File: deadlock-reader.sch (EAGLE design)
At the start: 57 parts, among them IC1 LM386M-1, IC2 STM32F072XX, IC3 MCP16301/H, IC4 MAX3232CSE, J1 RJ11-2X, X1 MINI-USB-SCHIELD-32005-301

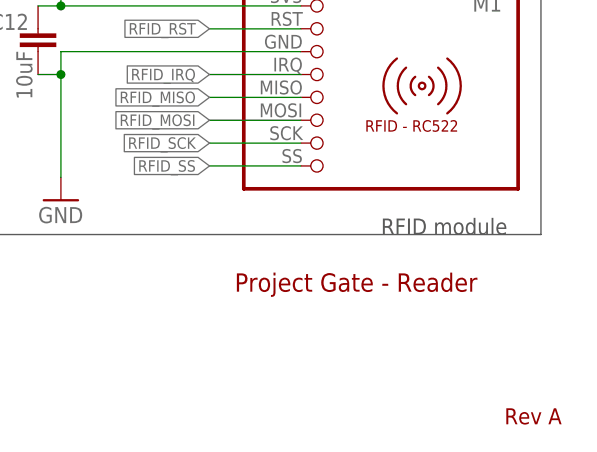
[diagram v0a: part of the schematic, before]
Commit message: Remove all occurences of name 'Gate'
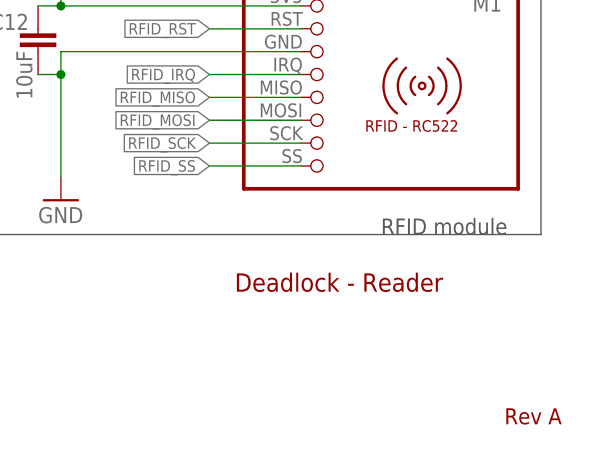
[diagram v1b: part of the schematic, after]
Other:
- note added: "Deadlock - Reader"
- note removed: "Project Gate - Reader"
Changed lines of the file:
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@@
 <?xml version="1.0" encoding="utf-8"?>
 <!DOCTYPE eagle SYSTEM "eagle.dtd">
-<eagle version="7.2.0">
+<eagle version="7.3.0">
 <drawing>
 <settings>
@@
 <sheet>
 <plain>
-<text x="217.424" y="20.32" size="2.032" layer="94" font="vector">Project Gate - Reader</text>
+<text x="217.424" y="20.32" size="2.032" layer="94" font="vector">Deadlock - Reader</text>
 <text x="247.396" y="5.588" size="1.778" layer="94" font="vector">Rev A</text>
 <wire x1="154.94" y1="170.18" x2="251.46" y2="170.18" width="0.1524" layer="97"/>

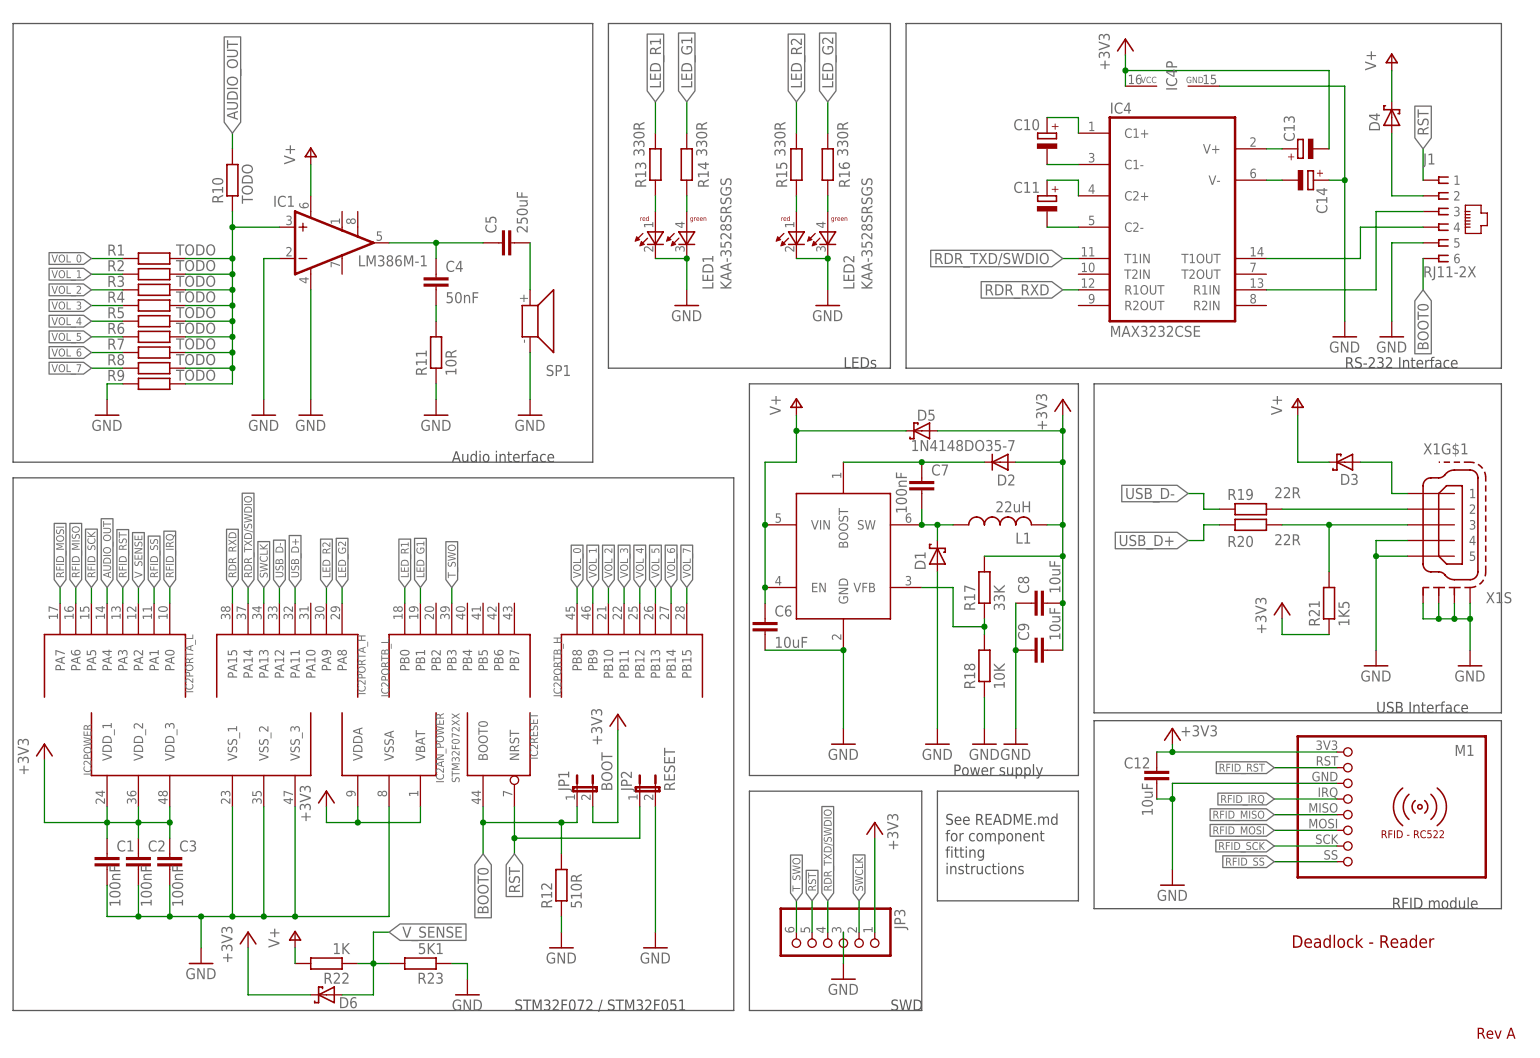
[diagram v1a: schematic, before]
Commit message: User trimmer to regulate audio volume instead of digital pot
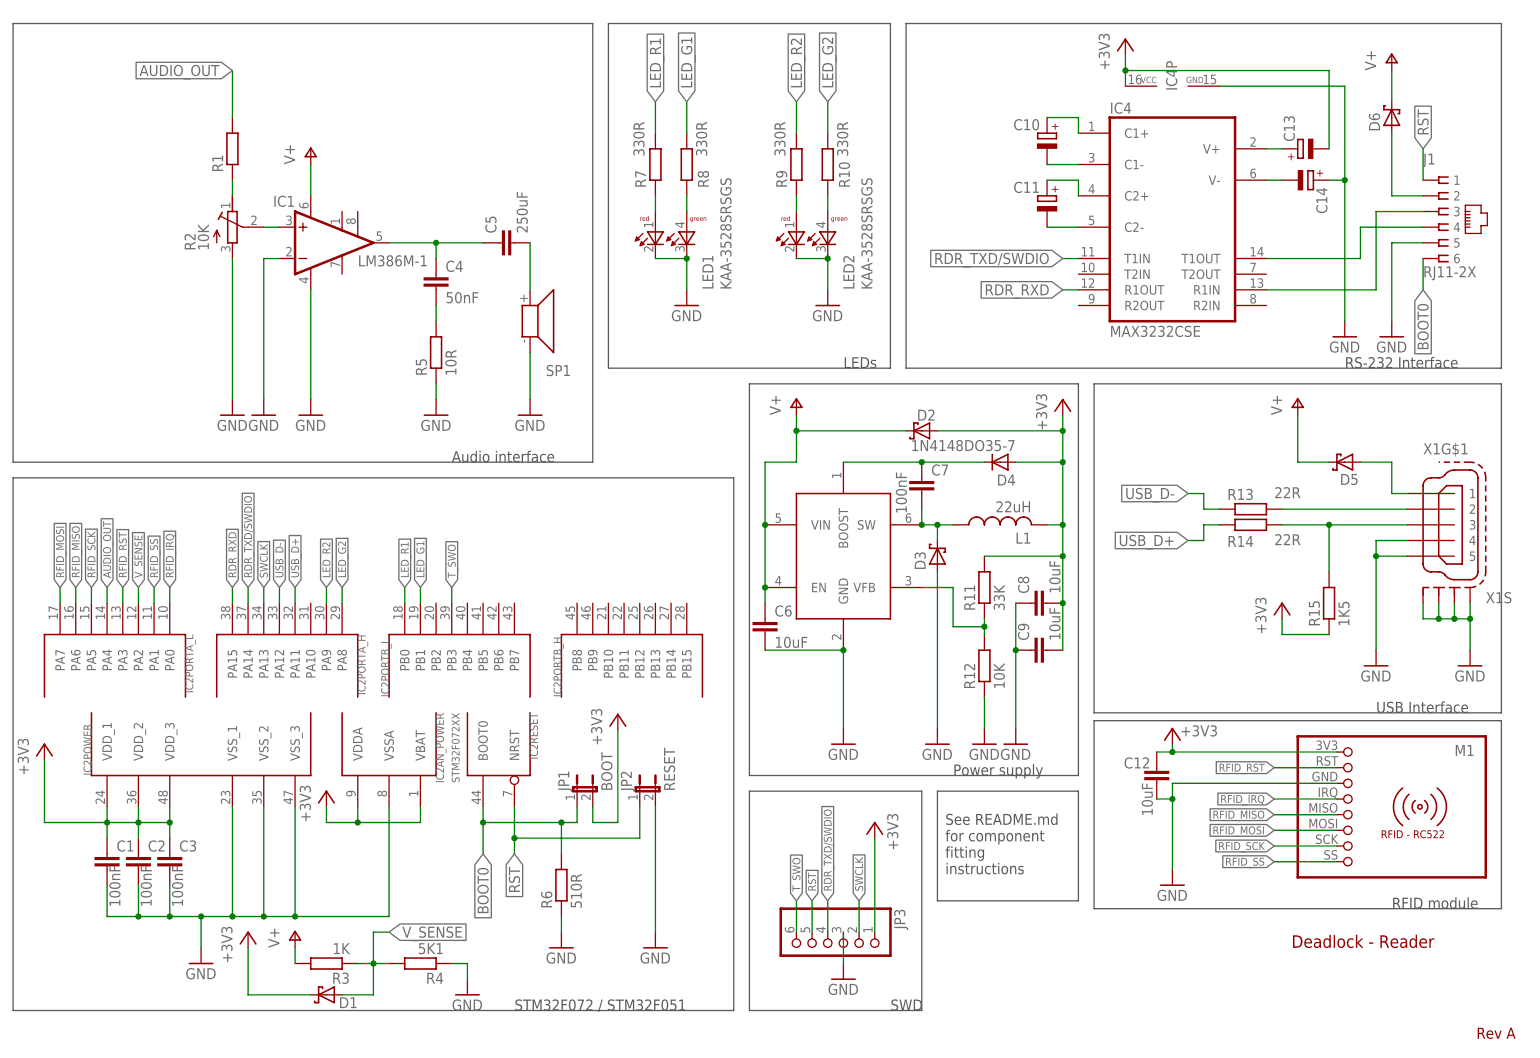
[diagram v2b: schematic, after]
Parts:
- removed R16: 330R, rcl:R-EU_R0805
- removed R17: 33K, rcl:R-EU_R0805
- removed R18: 10K, rcl:R-EU_R0805
- removed R19, R20: 22R, rcl:R-EU_R0805
- removed R21: 1K5, rcl:R-EU_R0805
- removed R22: 1K, rcl:R-EU_R0805
- removed R23: 5K1, rcl:R-EU_R0805
- D2: value 1N4148DO35-7 -> (none); device diode:1N4148DO35-7 -> diode:SCHOTTKY-DIODESMD
- D4: value (none) -> 1N4148DO35-7; device diode:SCHOTTKY-DIODESMD -> diode:1N4148DO35-7
- R1: value TODO -> (none); device rcl:R-EU_R0805 -> resistor:R-EU_M0805
- R10, R7, R8, R9: value TODO -> 330R
- R11: value 10R -> 33K
- R12: value 510R -> 10K
- R13, R14: value 330R -> 22R
- R15: value 330R -> 1K5
- R2: value TODO -> 10K; device rcl:R-EU_R0805 -> resistor:R-TRIMM3314J
- R3: value TODO -> 1K
- R4: value TODO -> 5K1
- R5: value TODO -> 10R
- R6: value TODO -> 510R
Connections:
- removed net VOL_0: IC2PORTB_H.PB8, R1.1
- removed net VOL_1: IC2PORTB_H.PB9, R2.1
- removed net VOL_2: IC2PORTB_H.PB10, R3.1
- removed net VOL_3: IC2PORTB_H.PB11, R4.1
- removed net VOL_4: IC2PORTB_H.PB12, R5.1
- removed net VOL_5: IC2PORTB_H.PB13, R6.1
- removed net VOL_6: IC2PORTB_H.PB14, R7.1
- removed net VOL_7: IC2PORTB_H.PB15, R8.1
- new net N$14: R1.1, R2.E
- net +3V3: now also D1.C, D4.A, R11.2, R15.1; no longer D5.A, D6.C, R17.2, R21.1
- net AUDIO_OUT: now also R1.2; no longer R10.2
- net BOOT0: now also R6.2; no longer R12.2
- net GND: now also D3.A, R2.A, R4.1, R5.1, R6.1; no longer D1.A, R11.1, R18.1, R23.1, R9.1
- net LED_G1: now also R8.2; no longer R14.2
- net LED_G2: now also R10.2; no longer R16.2
- net LED_R1: now also R7.2; no longer R13.2
- net LED_R2: now also R9.2; no longer R15.2
- net N$10: now also R9.1; no longer R15.1
- net N$11: now also D5.A; no longer D3.A
- net N$12: now also R13.2; no longer R19.2
- net N$13: now also R14.2, R15.2; no longer R20.2, R21.2
- net N$15: now also R2.S; no longer R1.2, R10.1, R2.2, R3.2, R4.2, R5.2, R6.2, R7.2, R8.2, R9.2
- net N$17: now also R5.2; no longer R11.2
- net N$19: now also R7.1; no longer R13.1
- net N$20: now also R8.1; no longer R14.1
- net N$21: now also R10.1; no longer R16.1
- net N$22: now also D3.C; no longer D1.C
- net N$23: now also D4.C; no longer D2.C
- net N$25: now also R11.1, R12.2; no longer R17.1, R18.2
- net N$9: now also D6.A; no longer D4.A
- net USB_D+: now also R14.1; no longer R20.1
- net USB_D-: now also R13.1; no longer R19.1
- net V+: now also D2.C, D6.C, R3.2; no longer D3.C, D4.C, R22.2
- net V_SENSE: now also D1.A, R3.1, R4.2; no longer D6.A, R22.1, R23.2
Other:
- moved on the sheet: D1, D3, D5, D6, R1, R10, R11, R12, R13, R14, R15, R3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

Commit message: Select components from distributor and adjust footprints
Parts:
- removed D6: (no value), diode:SCHOTTKY-DIODESMD
- added D7: BAT60J, diode:BAT60J
- C10, C11, C13, C14: value (none) -> 1uF; device rcl:CPOL-EU153CLV-0505 -> rcl:C-EUC0805
- C4: value 50nF -> 100nF
- C5: value 250uF -> 220uF; device rcl:C-EUC0805 -> rcl:CPOL-EUD
- C6: device rcl:C-EUC3225 -> rcl:CPOL-EUSMCD
- C8, C9: device rcl:C-EUC0805 -> rcl:CPOL-EUA/3216-18R
- D1, D2: value (none) -> BAT54; device diode:SCHOTTKY-DIODESMD -> diode:BAT54
- D3, D5: value (none) -> BAT60J; device diode:SCHOTTKY-DIODESMD -> diode:BAT60J
- D4: value 1N4148DO35-7 -> 1N4148; device diode:1N4148DO35-7 -> diode:DIODE-SOD323-W
- J1: value RJ11-2X -> RJ12 6p6c
- L1: value 22uH -> 15uH
- R1: value (none) -> 100K
- R2: device resistor:R-TRIMM3314J -> resistor:R-TRIMM3314G
- SP1: value SMS-1308MS-2-R -> KSS1201; device speaker:SMS-1308MS-2-R -> buzzer:KSS1201
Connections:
- net +3V3: now also C13.2, C8.+, C9.+; no longer C13.-, C8.2, C9.2
- net GND: now also C14.2, C6.-, C8.-, C9.-; no longer C14.+, C6.2, C8.1, C9.1
- net N$11: now also D7.A; no longer D5.A
- net N$16: now also C5.+; no longer C5.1
- net N$18: now also C5.-; no longer C5.2
- net N$3: now also C10.1; no longer C10.+
- net N$4: now also C10.2; no longer C10.-
- net N$5: now also C11.1; no longer C11.+
- net N$6: now also C11.2; no longer C11.-
- net N$7: now also C13.1; no longer C13.+
- net N$8: now also C14.1; no longer C14.-
- net N$9: now also D5.A; no longer D6.A
- net V+: now also C6.+, D7.C; no longer C6.1, D6.C
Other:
- moved on the sheet: C4, D5, IC1, R1, R2, R5

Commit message: Final component placement
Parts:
- C5: value 220uF -> 100uF; device rcl:CPOL-EUD -> rcl:C-EUC1206
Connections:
- net N$16: now also C5.1; no longer C5.+
- net N$18: now also C5.2; no longer C5.-
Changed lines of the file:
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@@
 <?xml version="1.0" encoding="utf-8"?>
 <!DOCTYPE eagle SYSTEM "eagle.dtd">
-<eagle version="7.3.0">
+<eagle version="7.4.0">
 <drawing>
 <settings>
@@
 <grid distance="0.1" unitdist="inch" unit="inch" style="lines" multiple="1" display="no" altdistance="0.01" altunitdist="inch" altunit="inch"/>
 <layers>
-<layer number="1" name="Top" color="4" fill="1" visible="yes" active="no"/>
-<layer number="16" name="Bottom" color="1" fill="1" visible="yes" active="no"/>
-<layer number="17" name="Pads" color="2" fill="1" visible="yes" active="no"/>
-<layer number="18" name="Vias" color="2" fill="1" visible="yes" active="no"/>
-<layer number="19" name="Unrouted" color="6" fill="1" visible="yes" active="no"/>
-<layer number="20" name="Dimension" color="15" fill="1" visible="yes" active="no"/>
-<layer number="21" name="tPlace" color="7" fill="1" visible="yes" active="no"/>
-<layer number="22" name="bPlace" color="7" fill="1" visible="yes" active="no"/>
-<layer number="23" name="tOrigins" color="15" fill="1" visible="yes" active="no"/>
-<layer number="24" name="bOrigins" color="15" fill="1" visible="yes" active="no"/>
-<layer number="25" name="tNames" color="7" fill="1" visible="yes" active="no"/>
-<layer number="26" name="bNames" color="7" fill="1" visible="yes" active="no"/>
-<layer number="27" name="tValues" color="7" fill="1" visible="yes" active="no"/>
-<layer number="28" name="bValues" color="7" fill="1" visible="yes" active="no"/>
+<layer number="1" name="Top" color="4" fill="1" visible="no" active="no"/>
+<layer number="16" name="Bottom" color="1" fill="1" visible="no" active="no"/>
+<layer number="17" name="Pads" color="2" fill="1" visible="no" active="no"/>
+<layer number="18" name="Vias" color="2" fill="1" visible="no" active="no"/>
+<layer number="19" name="Unrouted" color="6" fill="1" visible="no" active="no"/>
+<layer number="20" name="Dimension" color="15" fill="1" visible="no" active="no"/>
+<layer number="21" name="tPlace" color="7" fill="1" visible="no" active="no"/>
+<layer number="22" name="bPlace" color="7" fill="1" visible="no" active="no"/>
+<layer number="23" name="tOrigins" color="15" fill="1" visible="no" active="no"/>
+<layer number="24" name="bOrigins" color="15" fill="1" visible="no" active="no"/>
+<layer number="25" name="tNames" color="7" fill="1" visible="no" active="no"/>
+<layer number="26" name="bNames" color="7" fill="1" visible="no" active="no"/>
+<layer number="27" name="tValues" color="7" fill="1" visible="no" active="no"/>
+<layer number="28" name="bValues" color="7" fill="1" visible="no" active="no"/>
 <layer number="29" name="tStop" color="7" fill="3" visible="no" active="no"/>
 <layer number="30" name="bStop" color="7" fill="6" visible="no" active="no"/>
@@
 <layer number="35" name="tGlue" color="7" fill="4" visible="no" active="no"/>
 <layer number="36" name="bGlue" color="7" fill="5" visible="no" active="no"/>
-<layer number="37" name="tTest" color="7" fill="1" visible="yes" active="no"/>
-<layer number="38" name="bTest" color="7" fill="1" visible="yes" active="no"/>
+<layer number="37" name="tTest" color="7" fill="1" visible="no" active="no"/>
+<layer number="38" name="bTest" color="7" fill="1" visible="no" active="no"/>
 <layer number="39" name="tKeepout" color="4" fill="11" visible="no" active="no"/>
 <layer number="40" name="bKeepout" color="1" fill="11" visible="no" active="no"/>
@@
 <layer number="44" name="Drills" color="7" fill="1" visible="no" active="no"/>
 <layer number="45" name="Holes" color="7" fill="1" visible="no" active="no"/>
-<layer number="46" name="Milling" color="3" fill="1" visible="yes" active="no"/>
-<layer number="47" name="Measures" color="7" fill="1" visible="yes" active="no"/>
-<layer number="48" name="Document" color="7" fill="1" visible="yes" active="no"/>
-<layer number="49" name="Reference" color="7" fill="1" visible="yes" active="no"/>
-<layer number="50" name="dxf" color="7" fill="1" visible="yes" active="no"/>
-<layer number="51" name="tDocu" color="7" fill="1" visible="yes" active="no"/>
-<layer number="52" name="bDocu" color="7" fill="1" visible="yes" active="no"/>
-<layer number="53" name="tGND_GNDA" color="7" fill="9" visible="yes" active="no"/>
-<layer number="54" name="bGND_GNDA" color="1" fill="9" visible="yes" active="no"/>
-<layer number="56" name="wert" color="7" fill="1" visible="yes" active="no"/>
-<layer number="57" name="tCAD" color="7" fill="1" visible="yes" active="no"/>
+<layer number="46" name="Milling" color="3" fill="1" visible="no" active="no"/>
+<layer number="47" name="Measures" color="7" fill="1" visible="no" active="no"/>
+<layer number="48" name="Document" color="7" fill="1" visible="no" active="no"/>
+<layer number="49" name="Reference" color="7" fill="1" visible="no" active="no"/>
+<layer number="50" name="dxf" color="7" fill="1" visible="no" active="no"/>
+<layer number="51" name="tDocu" color="7" fill="1" visible="no" active="no"/>
+<layer number="52" name="bDocu" color="7" fill="1" visible="no" active="no"/>
+<layer number="53" name="tGND_GNDA" color="7" fill="9" visible="no" active="no"/>
+<layer number="54" name="bGND_GNDA" color="1" fill="9" visible="no" active="no"/>
+<layer number="56" name="wert" color="7" fill="1" visible="no" active="no"/>
+<layer number="57" name="tCAD" color="7" fill="1" visible="no" active="no"/>
 <layer number="90" name="Modules" color="5" fill="1" visible="yes" active="yes"/>
 <layer number="91" name="Nets" color="2" fill="1" visible="yes" active="yes"/>
@@
 <part name="R1" library="resistor" deviceset="R-EU_" device="M0805" value="100K"/>
 <part name="GND2" library="supply1" deviceset="GND" device=""/>
-<part name="C5" library="rcl" deviceset="CPOL-EU" device="D" value="220uF"/>
 <part name="C6" library="rcl" deviceset="CPOL-EU" device="SMCD" value="10uF"/>
 <part name="C8" library="rcl" deviceset="CPOL-EU" device="A/3216-18R" value="10uF"/>
@@
 <part name="D5" library="diode" deviceset="BAT60J" device=""/>
 <part name="SP1" library="buzzer" deviceset="KSS1201" device=""/>
+<part name="C5" library="rcl" deviceset="C-EU" device="C1206" value="100uF"/>
 </parts>
 <sheets>
@@
 <instance part="R1" gate="G$1" x="35.56" y="152.4" rot="R90"/>
 <instance part="GND2" gate="1" x="35.56" y="109.22"/>
-<instance part="C5" gate="G$1" x="78.74" y="137.16" rot="R90"/>
 <instance part="C6" gate="G$1" x="132.08" y="73.66"/>
 <instance part="C8" gate="G$1" x="177.8" y="76.2" rot="R270"/>
@@
 </instance>
 <instance part="SP1" gate="1" x="83.82" y="124.46" rot="R270"/>
+<instance part="C5" gate="G$1" x="78.74" y="137.16" rot="R90"/>
 </instances>
 <busses>
@@
 <wire x1="68.58" y1="134.62" x2="68.58" y2="137.16" width="0.1524" layer="91"/>
 <junction x="68.58" y="137.16"/>
-<pinref part="C5" gate="G$1" pin="+"/>
+<pinref part="C5" gate="G$1" pin="1"/>
 </segment>
 </net>
@@
 <segment>
 <wire x1="83.82" y1="137.16" x2="83.82" y2="129.54" width="0.1524" layer="91"/>
-<pinref part="C5" gate="G$1" pin="-"/>
 <pinref part="SP1" gate="1" pin="1"/>
-</segment>
-</net>
+<pinref part="C5" gate="G$1" pin="2"/>
+</segment>
+</net>
